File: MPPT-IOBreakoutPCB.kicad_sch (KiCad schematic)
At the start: 0 parts

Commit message: wrong schem
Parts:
- added 120m/s1: Microphone_Condenser, Resistor_SMD:R_0603_1608Metric, symbol Device:Microphone_Condenser
- added J3, J4, J5: Conn_01x06, UTSVT_Connectors:Molex_Microfit3.0_02x03_6-Pin-Vertical-PCB-Receptacle_447690601, symbol Connector_Generic:Conn_01x06
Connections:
- new net +12V: J3.1 (Pin_1), J5.1 (Pin_1)
- new net CAN_H-in: J3.4 (Pin_4), J5.3 (Pin_3)
- new net CAN_H-out: 120m/s1.1 (-), J4.4 (Pin_4), J5.5 (Pin_5)
- new net CAN_L-in: J3.5 (Pin_5), J5.4 (Pin_4)
- new net CAN_L-out: 120m/s1.2 (+), J4.5 (Pin_5), J5.6 (Pin_6)
- new net GND: J3.2 (Pin_2), J5.2 (Pin_2)
- no-connect marks 0 -> 6

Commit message: right schem
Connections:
- net +12V: now also J3.3 (Pin_3); no longer J3.1 (Pin_1)
- net CAN_H-in: now also J3.6 (Pin_6); no longer J3.4 (Pin_4)
- net CAN_H-out: now also J4.6 (Pin_6); no longer J4.4 (Pin_4)
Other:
- moved on the sheet: J5

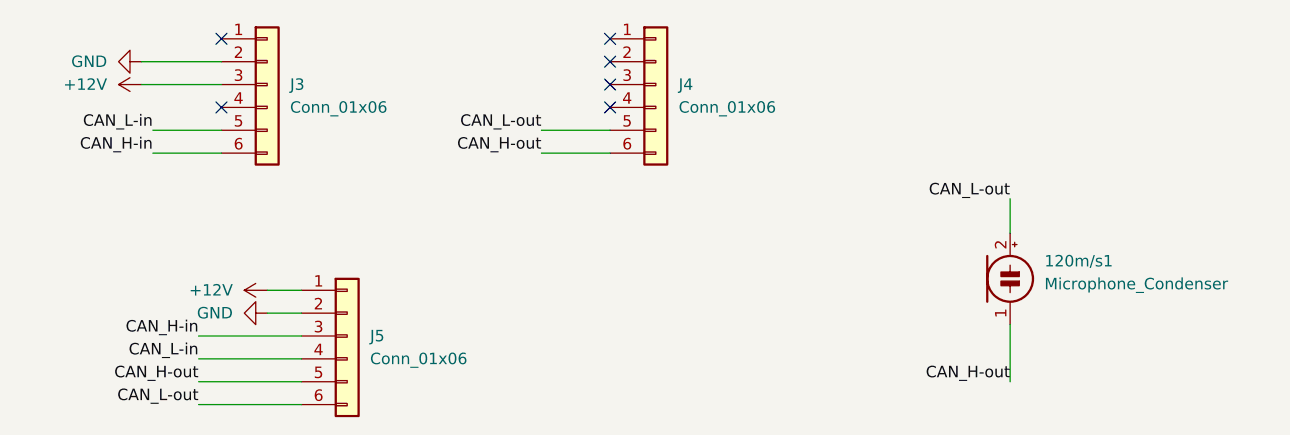
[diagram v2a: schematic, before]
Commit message: mppt matched schem
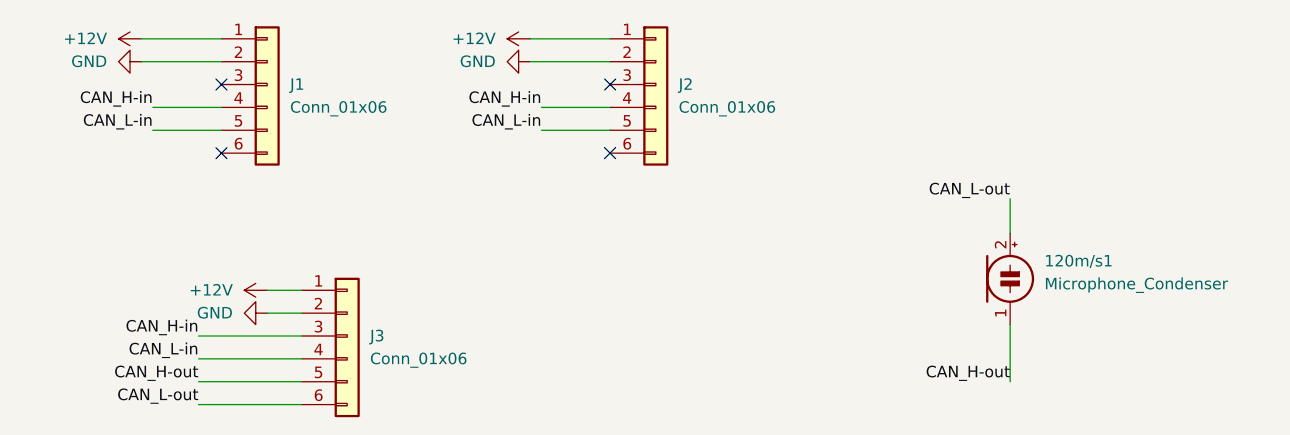
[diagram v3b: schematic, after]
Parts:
- renumbered J3 to J1, J4 to J2, J5 to J3
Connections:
- net +12V: now also J1.1 (Pin_1), J2.1 (Pin_1); no longer J1.3 (Pin_3)
- net CAN_H-in: now also J1.4 (Pin_4), J2.4 (Pin_4); no longer J1.6 (Pin_6)
- net CAN_H-out: no longer J2.6 (Pin_6)
- net CAN_L-in: now also J2.5 (Pin_5)
- net CAN_L-out: no longer J2.5 (Pin_5)
- net GND: now also J2.2 (Pin_2)
- no-connect marks 6 -> 4

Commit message: layout maybe done
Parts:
- J3: footprint UTSVT_Connectors:Molex_Microfit3.0_02x03_6-Pin-Vertical-PCB-Receptacle_447690601 -> footprints:CONN_SD-44764-001_06_MOL
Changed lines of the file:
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@@
 			)
 		)
-		(property "Footprint" "UTSVT_Connectors:Molex_Microfit3.0_02x03_6-Pin-Vertical-PCB-Receptacle_447690601"
+		(property "Footprint" "footprints:CONN_SD-44764-001_06_MOL"
 			(at 73.66 72.39 0)
 			(effects

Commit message: traces
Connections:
- net CAN_H-in: no longer J2.4 (Pin_4)
- net CAN_H-out: now also J2.4 (Pin_4)
- net CAN_L-in: no longer J2.5 (Pin_5)
- net CAN_L-out: now also J2.5 (Pin_5)
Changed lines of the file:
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@@
 		)
 	)
-	(label "CAN_H-in"
+	(label "CAN_H-out"
 		(at 95.25 46.99 180)
 		(effects
@@
 		)
 	)
-	(label "CAN_L-in"
+	(label "CAN_L-out"
 		(at 95.25 49.53 180)
 		(effects
